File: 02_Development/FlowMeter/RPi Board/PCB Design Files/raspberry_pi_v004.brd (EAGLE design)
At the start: 111.8 x 128.3 mm, 116 parts, among them J5 POWER_JACK, P1 SPL006-007, P2 SPL006-007, P3 SPL006-007, P4 SPL006-007, P5 SPL006-007, Q1 4.3A/20V/54mΩ, Q2 500mA/300V, U6 TCA9548APWR, U7 TCA9548APWR

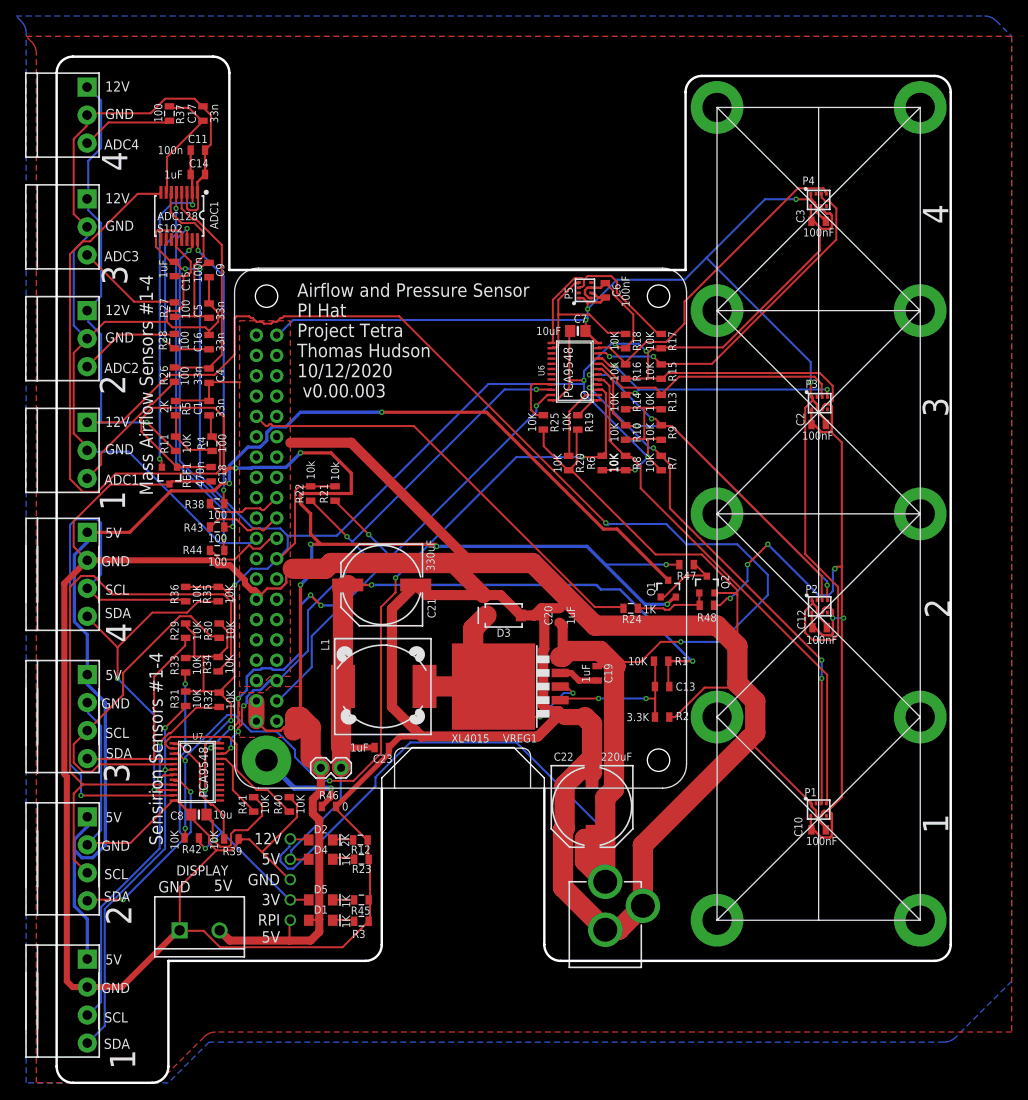
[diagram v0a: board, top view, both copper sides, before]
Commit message: updated PCB with new 5V regulator (#145)
* added new 5V regulator

added new 5V regulator as existing regulator was out-of-stock at JLCPCB

* updated capacitor

changed C22 and C25 to 1206 footprint and specified 2mohm low ESR cap
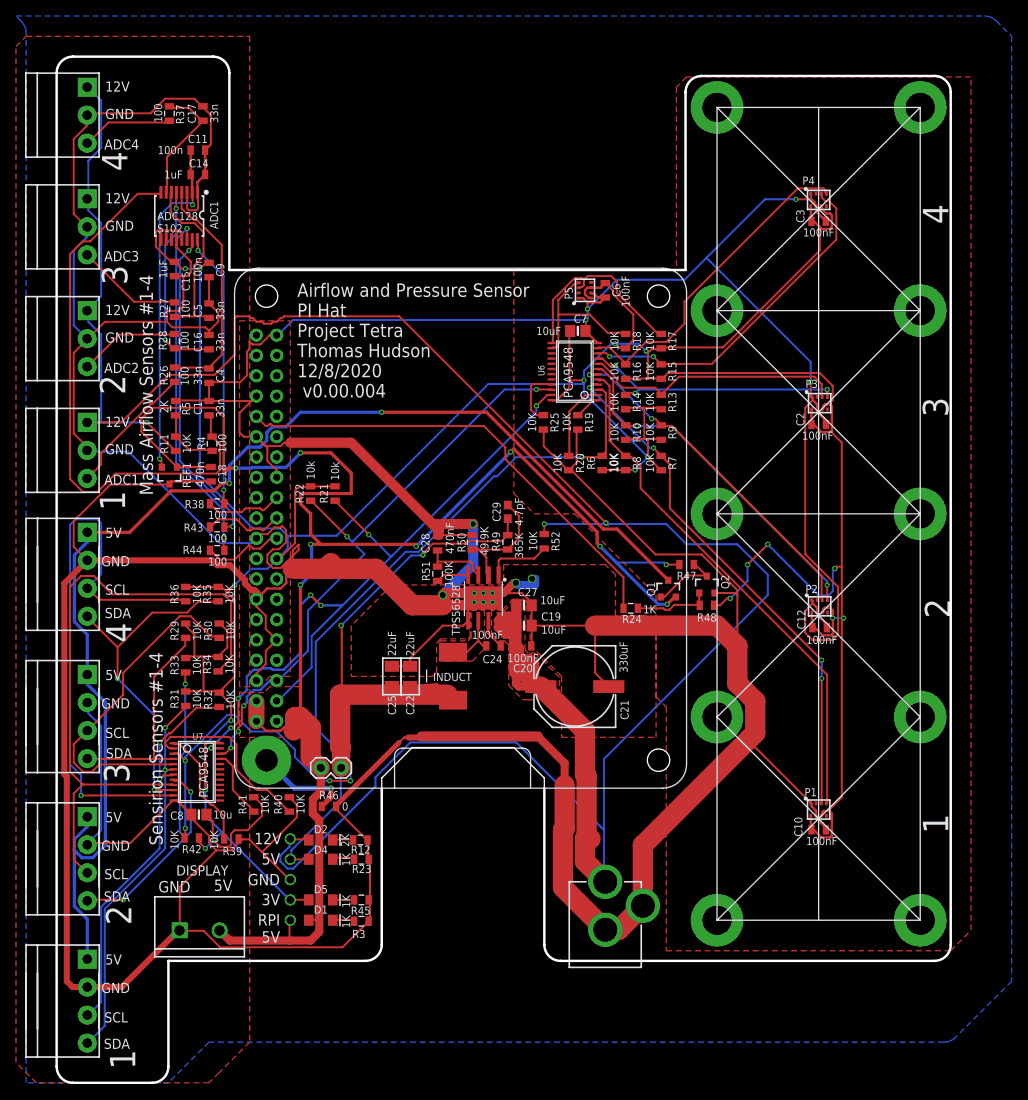
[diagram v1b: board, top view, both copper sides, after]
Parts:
- removed C13: 33n, SparkFun-Capacitors:0805
- removed C23: 1uF, SparkFun-Capacitors:0805
- removed D3: 3A/40V/500mV, SparkFun-DiscreteSemi:SMA-DIODE
- removed L1: INDUCTOR12.5, th_libraries:INDUCTOR_12.5X12.5
- removed R1: 10K, SparkFun-Resistors:0805
- removed R2: 3.3K, SparkFun-Resistors:0805
- removed VREG1: XL4015, th_libraries:TO263-5
- added C24: 100nF, SparkFun-Capacitors:0805
- added C25: 22uF, microbuilder:_1206
- added C27: 10uF, microbuilder:0805-NO
- added C28: 470nF, SparkFun-Capacitors:0805
- added C29: 4.7pF, SparkFun-Capacitors:0603
- added INDUCT: INDUCTOR_6.6_7.3, th_libraries:INDUCTOR_6.6_7.3
- added R49: 365K, SparkFun-Passives:0805
- added R50: 49.9K, SparkFun-Passives:0805
- added R51: 100K, SparkFun-Passives:0805
- added R52: 10K, SparkFun-Resistors:0805
- added TPS: TPS56528, th_libraries:SOIC8_POWER
- C19: value 1uF -> 10uF; device SparkFun-Capacitors:0805 -> microbuilder:0805-NO
- C20: value 1uF -> 100nF
- C22: value 220uF -> 22uF; device SparkFun-Capacitors:PANASONIC_G -> microbuilder:_1206
- moved C22 27.9 mm to (13.7, -20.3), turned to 90 degrees
- moved C21 27.3 mm to (34.3, -21.6)
- moved C19 10.9 mm to (27.9, -14.0), turned to 0 degrees
- moved C20 5.85 mm to (27.9, -16.5), turned to 0 degrees
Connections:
- new net N$14: C24.1, TPS.7
- new net N$17: R51.1, TPS.4
- new net N$27: R52.2, TPS.1
- net 12V: now also C21.+, C27.1, R52.1, TPS.8; no longer C22.+, VREG1.5
- net 5V: now also C22.1, C25.1, C29.1, INDUCT.2, R49.2; no longer C13.1, C21.+, C23.1, L1.1, R1.1
- net GND: now also C19.2, C22.2, C25.2, C27.2, C28.2, R50.2, TPS.5, TPS.9; no longer C22.-, C23.2, D3.A, R2.2, VREG1.1
- net N$11: now also C29.2, R49.1, R50.1, TPS.2; no longer C13.2, R1.2, R2.1, VREG1.2
- net N$6: now also C24.2, INDUCT.1, TPS.6; no longer D3.C, L1.2, VREG1.3, VREG1.6
- net N$7: now also C28.1, R51.2, TPS.3; no longer C19.2, VREG1.4
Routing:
- net 12V: track 304.9 -> 355.7 mm
- net GND: track 900.3 -> 948.0 mm, vias 4 -> 14
- net N$6: track 34.7 -> 7.53 mm, vias 2 -> 0
- net 5V: track 97.9 -> 85.1 mm
- net PI_5V_POWER: track 202.1 -> 211.8 mm, vias 7 -> 9
- net N$27: track 0.00 -> 8.15 mm
- net N$11: track 21.5 -> 14.9 mm, vias 2 -> 0
- net RESET: track 108.2 -> 112.8 mm
- net N$17: track 0.00 -> 4.12 mm
- net N$14: track 0.00 -> 3.79 mm
- net GPIO12: track 56.0 -> 59.4 mm
- net N$7: track 5.02 -> 8.17 mm
- added copper zone on layer 1, net 12V
- added copper zone on layer 1, net N$6
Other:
- board text added: "Airflow and Pressure Sensor PI Hat Project Tetra Thomas Hudson 12/8/2020 v0.00.004"
- board text removed: "Airflow and Pressure Sensor PI Hat Project Tetra Thomas Hudson 10/12/2020 v0.00.003"

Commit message: Next revision of PCB (#152)
* Next revision of PCB

Changed I2C pullup resistors to 3Kohm

General tidy up and fix of issues on the PCB. Tweaked some polygons to eliminate sharp corners, made some traces larger.

* Changes made as per PR152

Changes made as requested, I also updated the pdf of the schematic and the dru file.

One thing I have noticed is that generating the BOM automatically comes up with the incorrect resistor value of 0.3 Ohms. I suspect this is to do with the library that is being used.

* Create READ ME BEFORE CONTINUING.md

Added a cautionary text file to explain the issue with the automatically generated BOM and the incorrect resistor values being utilised.
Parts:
- R10, R13, R14, R15, R16, R17, R18, R29, R30, R31, R32, R33, R34, R35, R36, R7, R8, R9: value 10K -> 3K
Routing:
- net 12V: track 355.7 -> 307.9 mm
- net 5V: track 85.1 -> 57.8 mm
- net GND: track 948.0 -> 948.9 mm
- added copper zone on layer 1, net 5V
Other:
- board text added: "Airflow and Pressure Sensor PI Hat Project Tetra Thomas Hudson 14/12/2020 v0.00.005"
- board text removed: "Airflow and Pressure Sensor PI Hat Project Tetra Thomas Hudson 12/8/2020 v0.00.004"
